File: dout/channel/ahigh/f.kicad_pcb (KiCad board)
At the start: 2 copper layers, 19.1 x 10.8 mm, 7 parts, among them J1 dio_channel_i, Q1 BC807, U1 LTV-357T

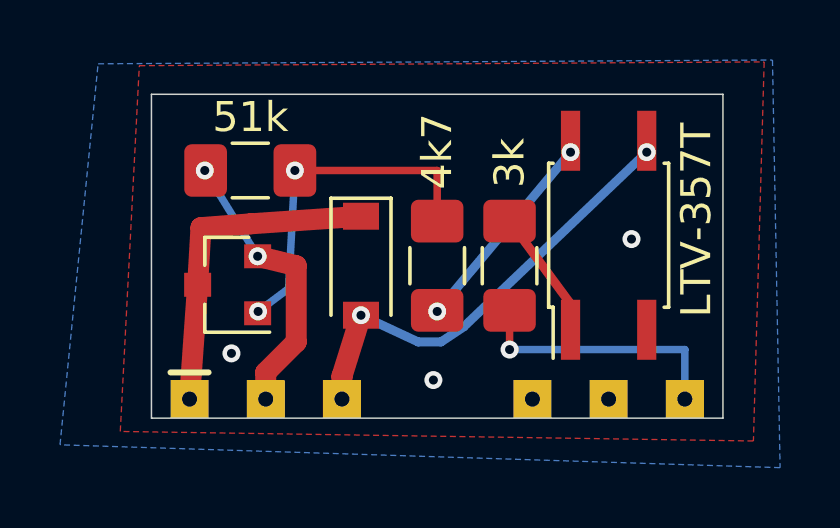
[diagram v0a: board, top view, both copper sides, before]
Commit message: voltage regulator for each module
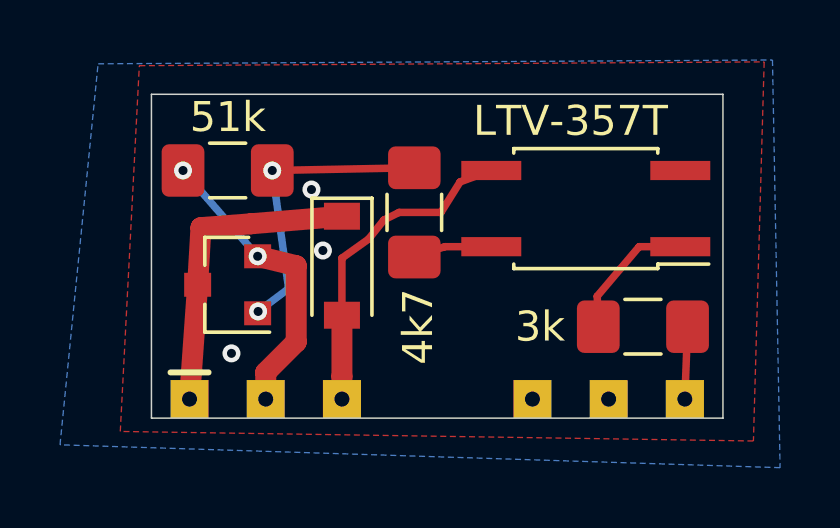
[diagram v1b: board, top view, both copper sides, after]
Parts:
- moved R3 4.89 mm to (177.7, 126.5), turned to 0 degrees
- moved R2 1.93 mm to (170.1, 122.7)
- moved U1 1.17 mm to (175.8, 122.6), turned to 180 degrees
- moved R1 0.75 mm to (163.8, 121.3)
- moved D1 0.64 mm to (167.6, 124.5)
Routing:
- net IN: track 8.80 -> 2.41 mm, vias 1 -> 0
- net Net-(R2-Pad2): track 6.92 -> 2.62 mm, vias 2 -> 0
- net VINM: track 15.1 -> 10.9 mm, vias 2 -> 0
- net Net-(Q1-Pad1): track 11.6 -> 9.98 mm
- net OUT: track 11.1 -> 10.4 mm
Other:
- board text added: "active high out"
- board text removed: "active high"
